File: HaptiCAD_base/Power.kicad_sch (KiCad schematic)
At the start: 6 parts, among them U501 AP2112K-3.3

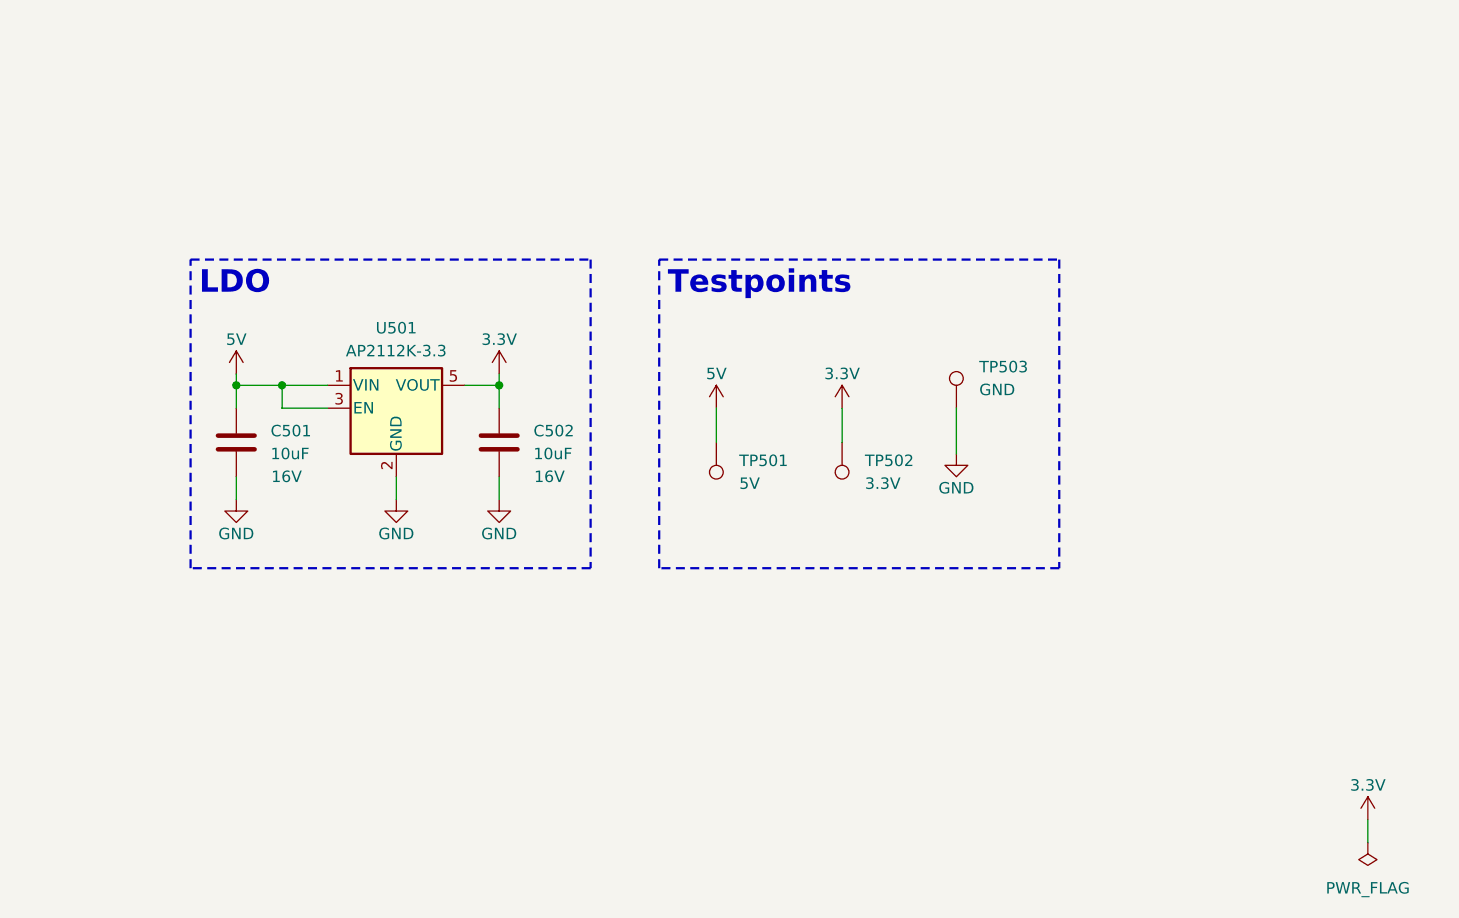
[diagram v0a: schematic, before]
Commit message: updated base schematic and PCB
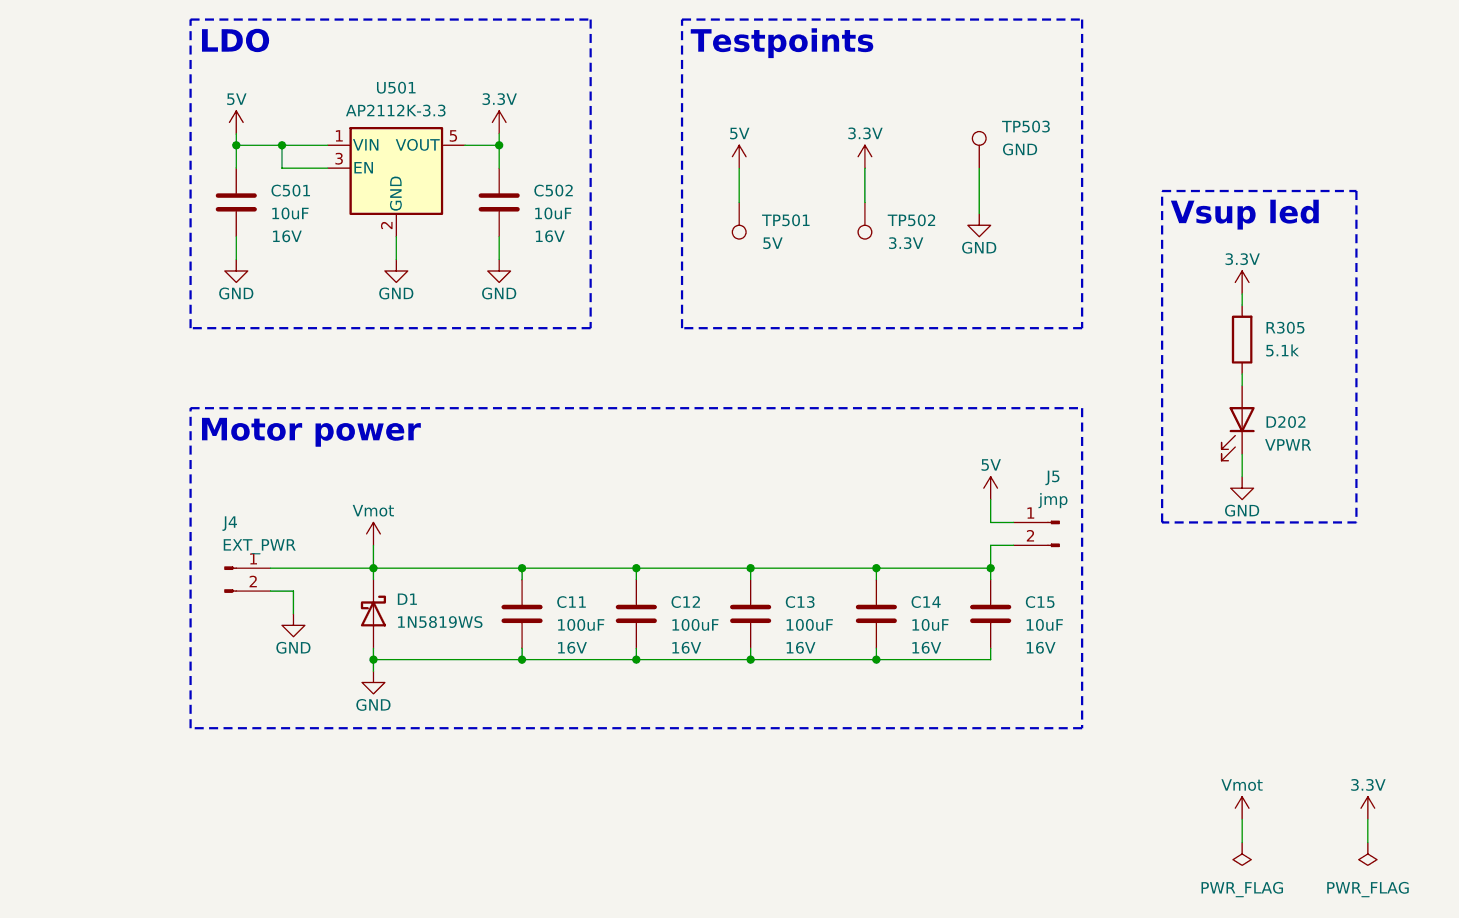
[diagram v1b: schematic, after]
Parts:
- added C11, C12, C13: 100uF, Capacitor_SMD:C_1206_3216Metric, symbol Device:C
- added C14, C15: 10uF, Capacitor_SMD:C_1206_3216Metric, symbol Device:C
- added D1: 1N5819WS, Diode_SMD:D_SOD-323_HandSoldering, symbol Diode:1N5819WS
- added D202: VPWR, Diode_SMD:D_0603_1608Metric, symbol Device:LED
- added J4: EXT_PWR, symbol Connector:Conn_01x02_Pin
- added J5: jmp, symbol Connector:Conn_01x02_Pin
- added R305: 5.1k, Resistor_SMD:R_0402_1005Metric, symbol Device:R
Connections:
- net 3.3V: now also R305.2
- net 5V: now also J5.1 (Pin_1)
- net GND: now also C11.2, C12.2, C13.2, C14.2, C15.2, D1.2 (A), D202.1 (K), J4.2 (Pin_2)
- new net: D202.2 (A), R305.1
- new net Vmot: C11.1, C12.1, C13.1, C14.1, C15.1, D1.1 (K), J4.1 (Pin_1), J5.2 (Pin_2)
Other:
- moved on the sheet: C501, C502, TP501, TP502, TP503, U501

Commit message: Finished schematic of the base board
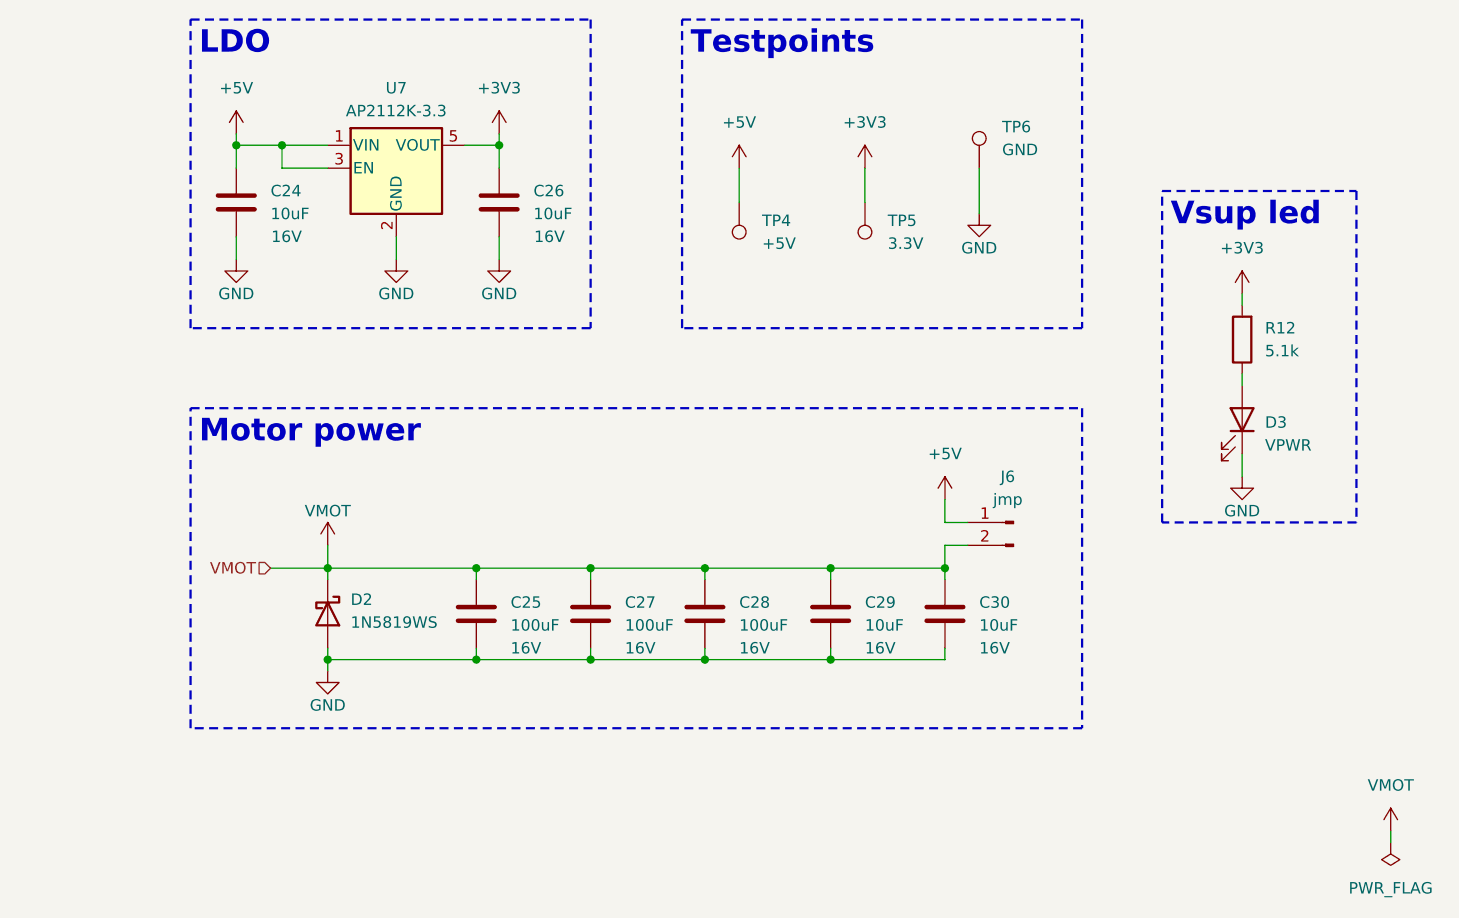
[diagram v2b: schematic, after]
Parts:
- removed J4: EXT_PWR, symbol Connector:Conn_01x02_Pin
- removed TP501: 5V, TestPoint:TestPoint_Pad_D1.0mm, symbol Connector:TestPoint
- added TP4: +5V, TestPoint:TestPoint_Pad_D1.0mm, symbol Connector:TestPoint
- renumbered C501 to C24, C11 to C25, C502 to C26, C12 to C27, C13 to C28, C14 to C29, C15 to C30, D1 to D2, D202 to D3, J5 to J6, R305 to R12, TP502 to TP5, TP503 to TP6, U501 to U7
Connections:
- net 3.3V renamed +3V3
- net 5V renamed +5V
- net +5V: now also TP4.1
- net Vmot renamed VMOT
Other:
- moved on the sheet: C25, C27, C28, C29, C30, D2, J6

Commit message: Finished the layout for the base and motor mount
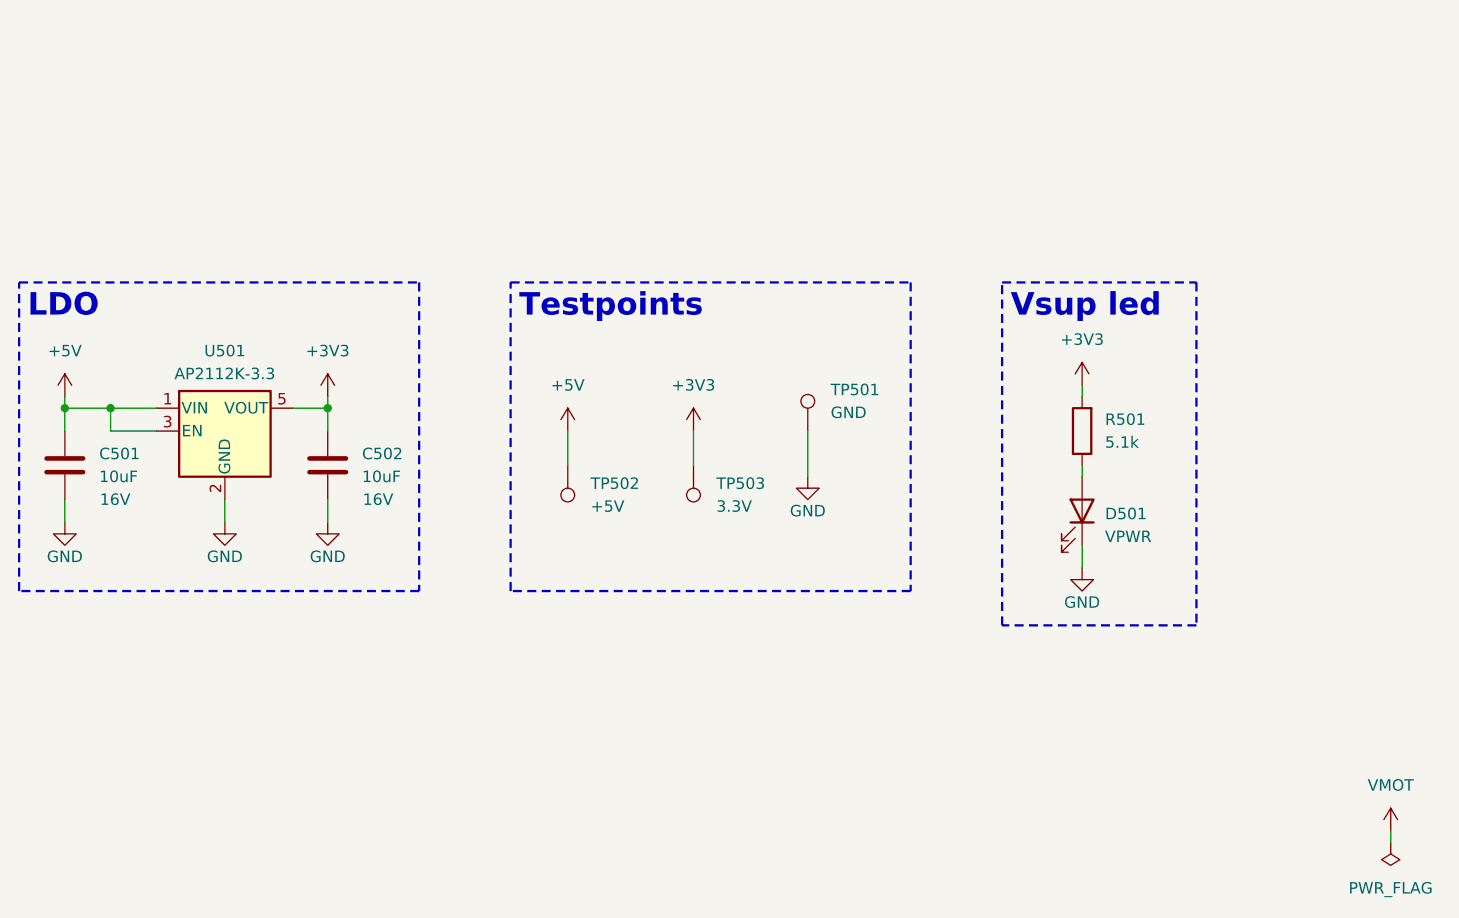
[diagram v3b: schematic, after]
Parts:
- removed C25, C27, C28: 100uF, Capacitor_SMD:C_1206_3216Metric, symbol Device:C
- removed C29, C30: 10uF, Capacitor_SMD:C_1206_3216Metric, symbol Device:C
- removed D2: 1N5819WS, Diode_SMD:D_SOD-323_HandSoldering, symbol Diode:1N5819WS
- removed J6: jmp, symbol Connector:Conn_01x02_Pin
- renumbered C24 to C501, C26 to C502, D3 to D501, R12 to R501, TP6 to TP501, TP4 to TP502, TP5 to TP503, U7 to U501
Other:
- moved on the sheet: C501, C502, D501, R501, TP501, TP502, TP503, U501
